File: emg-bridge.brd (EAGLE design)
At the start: 76.2 x 50.8 mm, 24 parts, among them J1 RJ25_4X1, J2 RJ25_4X1, J3 M03_0.156IN-RA, U1 ADM660ARZ

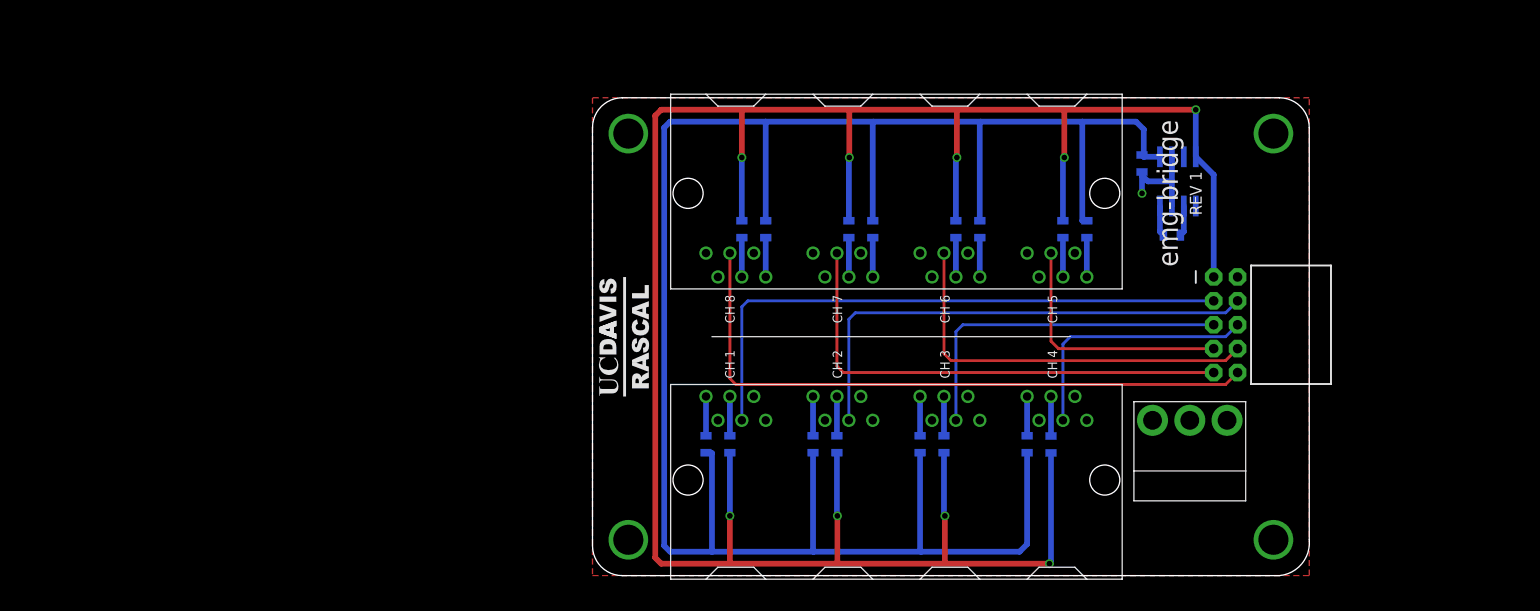
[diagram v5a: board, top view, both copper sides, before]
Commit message: Realization: the MC USB-1608G DAQ can only output 10mA for power, so the power circuitry has been completely reworked. Now with 3kV isolation!
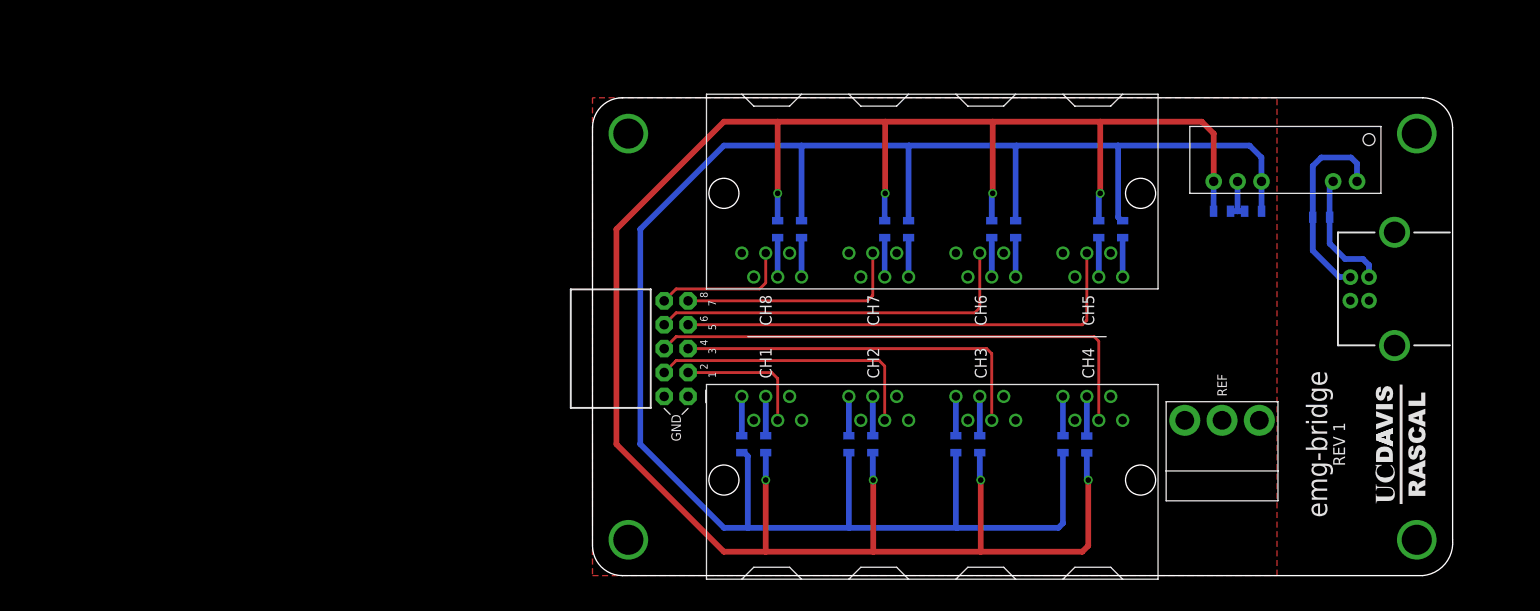
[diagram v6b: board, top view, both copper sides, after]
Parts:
- removed U1: ADM660ARZ, eagle-lib:SOIC8
- added C3: 0.1uF, SparkFun-Capacitors:0805
- added JP2: USB-B, SparkFun-Connectors:USB-B-PTH
- added U2: DC_ISOLATOR-RKZ0505D, eagle-lib:SIP7
- C1, C2: value 10uF -> 0.1uF
- moved U$1 83.3 mm to (86.0, 14.0)
- moved JP1 58.5 mm to (8.89, 24.1), turned to 180 degrees
- moved C1 16.0 mm to (77.5, 38.1), turned to 180 degrees
- moved C2 9.91 mm to (66.9, 38.7), turned to 180 degrees
- moved J2 3.81 mm to (58.3, 40.6)
- moved R10 3.81 mm to (56.4, 36.8)
- moved R12 3.81 mm to (45.0, 36.8)
- moved R16 3.81 mm to (22.2, 36.8)
- moved R4 3.81 mm to (27.3, 14.0)
- moved R5 3.81 mm to (41.2, 14.0)
- moved R6 3.81 mm to (38.6, 14.0)
- moved R8 3.81 mm to (50.0, 14.0)
- moved R9 3.81 mm to (53.8, 36.8)
- moved J1 3.81 mm to (14.0, 10.2)
- moved R2 3.81 mm to (15.9, 14.0)
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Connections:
- net +VE: now also C2.1, U2.7; no longer JP1.1, U1.8
- net -VE: now also C3.2, U2.5; no longer C2.1, U1.5
- net GND: now also C3.1, JP1.1, U2.6; no longer U1.3, U1.6
- net N$2: now also C1.1, JP2.VBUS, U2.1; no longer C1.2, U1.4
- net N$4: now also C1.2, JP2.GND, U2.2; no longer C1.1, U1.2
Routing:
- net CH8: track 68.1 -> 14.8 mm
- net CH1: track 62.5 -> 14.2 mm
- net CH7: track 52.4 -> 24.4 mm
- net CH4: track 27.5 -> 55.3 mm
- net CH2: track 52.9 -> 30.0 mm
- net CH5: track 27.0 -> 49.7 mm
- net +VE: track 260.1 -> 238.9 mm, vias 9 -> 8
- net N$2: track 3.25 -> 21.4 mm
- net -VE: track 224.8 -> 211.9 mm
- net N$4: track 3.25 -> 13.2 mm
- net GND: track 10.9 -> 4.68 mm, vias 1 -> 0
- net CH6: track 42.7 -> 40.1 mm
- net CH3: track 37.1 -> 39.6 mm
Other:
- board size 76.2 x 50.8 mm -> 91.5 x 50.8 mm
- board text added: "1"
- board text added: "2"
- board text added: "3"
- board text added: "4"
- board text added: "5"
- board text added: "6"
- board text added: "7"
- board text added: "8"
- board text added: "CH1"
- board text added: "CH2"
- board text added: "CH3"
- board text added: "CH4"
- board text added: "CH5"
- board text added: "CH6"
- board text added: "CH7"
- board text added: "CH8"
- board text added: "GND"
- board text added: "REF"
- board text removed: "CH 1"
- board text removed: "CH 2"
- board text removed: "CH 3"
- board text removed: "CH 4"
- board text removed: "CH 5"
- board text removed: "CH 6"
- board text removed: "CH 7"
- board text removed: "CH 8"

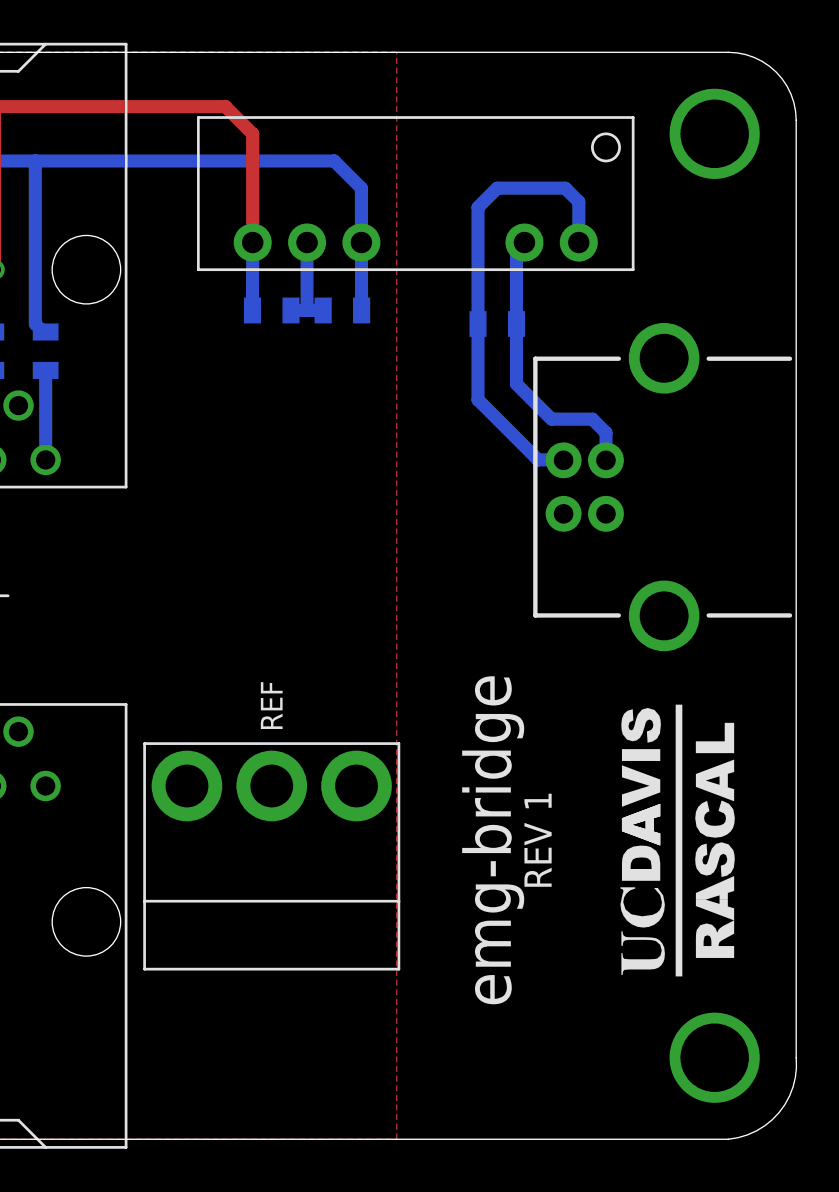
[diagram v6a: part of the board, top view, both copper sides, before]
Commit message: Added power jack.
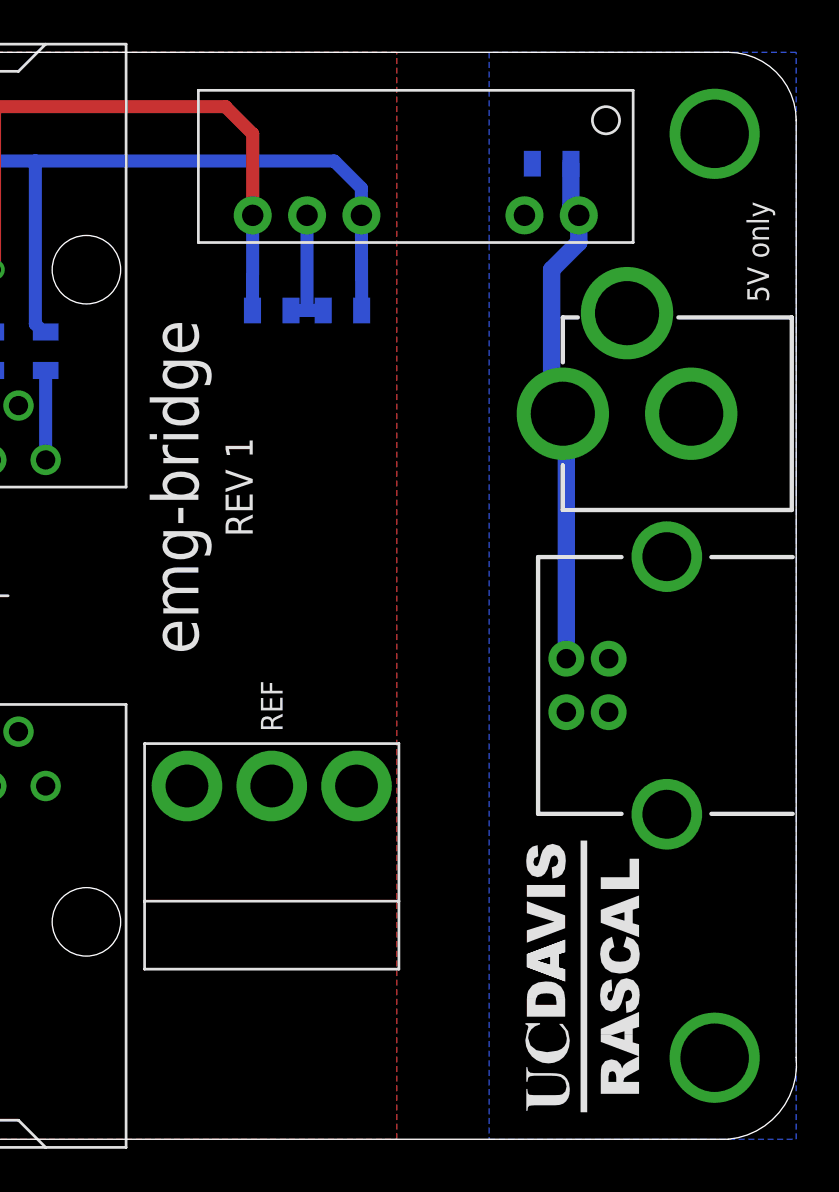
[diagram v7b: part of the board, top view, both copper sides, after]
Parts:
- removed JP2: USB-B, SparkFun-Connectors:USB-B-PTH
- removed U2: DC_ISOLATOR-RKZ0505D, eagle-lib:SIP7
- added J4: POWER_JACKPTH, SparkFun-Connectors:POWER_JACK_PTH
- added J5: USB-B, SparkFun-Connectors:USB-B-PTH
- added U1: DC_ISOLATOR-RKZ0505D, eagle-lib:SIP7
- moved C1 7.91 mm to (80.0, 45.6), turned to 0 degrees
- moved U$1 7.75 mm to (81.5, 7.62)
- renumbered JP1 to J6
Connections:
- removed net N$4: C1.2, JP2.GND, U2.2
- new net DGND: C1.2, J4.GND, J5.GND, U1.2
- net +VE: now also U1.7; no longer U2.7
- net -VE: now also U1.5; no longer U2.5
- net GND: now also U1.6; no longer U2.6
- net N$2: now also J4.PWR, J5.VBUS, U1.1; no longer JP2.VBUS, U2.1
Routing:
- net N$4: track 13.2 -> 0.00 mm
- net N$2: track 21.4 -> 24.1 mm
- net GND: track 4.68 -> 5.95 mm
- added copper zone on layer 16, net DGND
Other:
- board text added: "5V only"

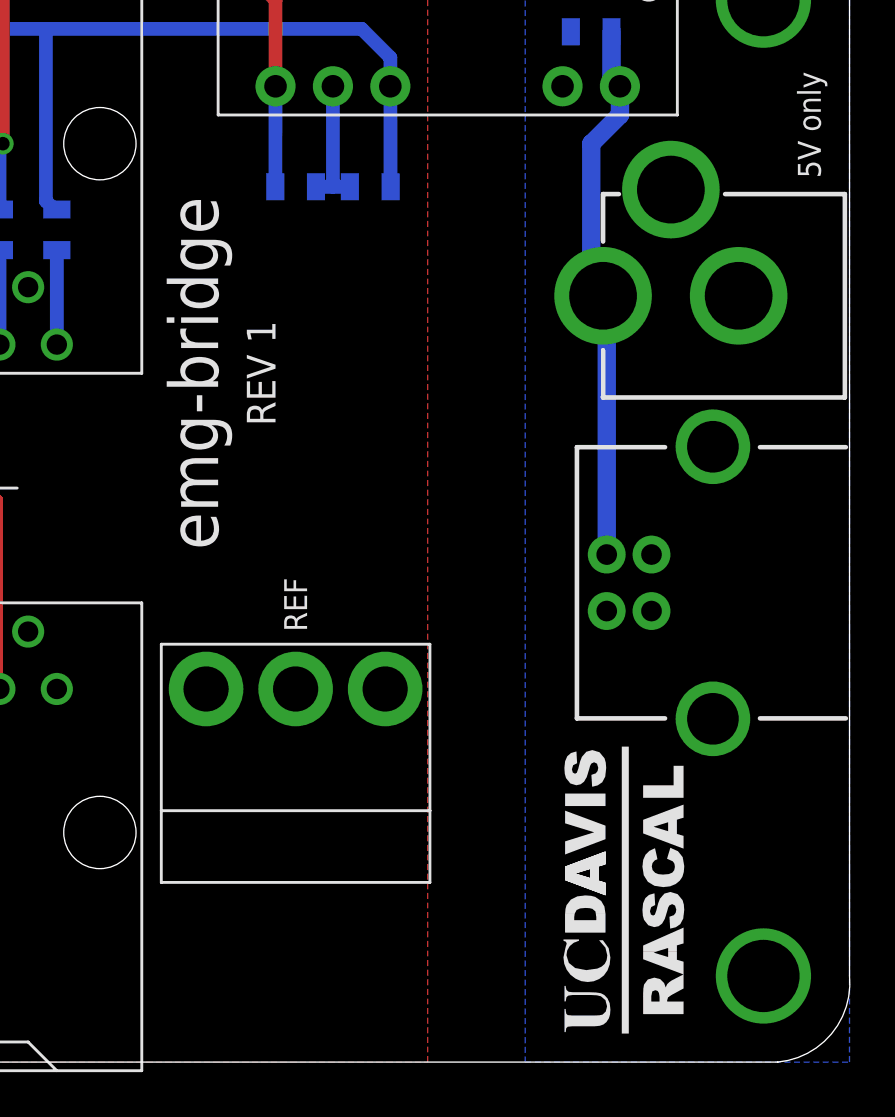
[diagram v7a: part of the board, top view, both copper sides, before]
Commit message: Added LED.
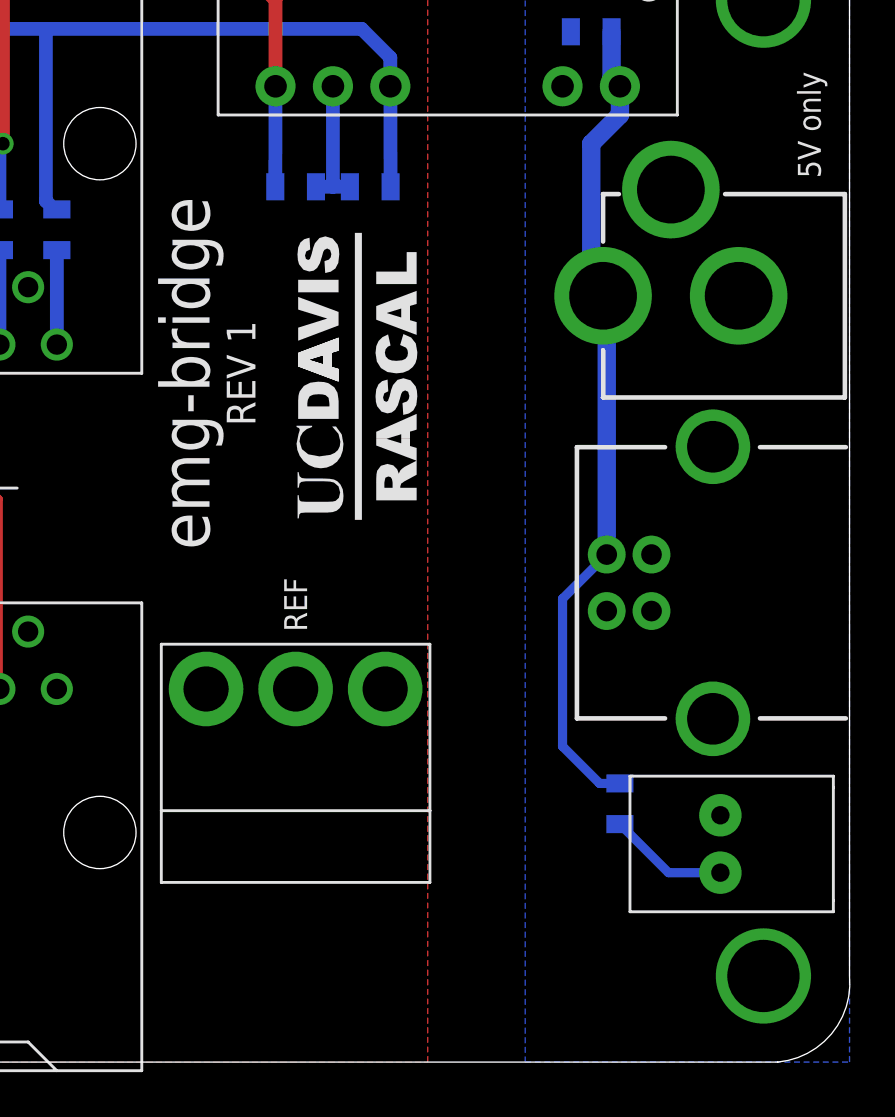
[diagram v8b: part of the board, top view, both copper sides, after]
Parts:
- added D1: LED_LA93B, eagle-lib:LED_RA
- added R17: (no value), SparkFun-Passives:0805
- moved U$1 25.6 mm to (69.7, 30.4)
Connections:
- new net N$4: D1.A, R17.1
- net DGND: now also D1.K
- net N$2: now also R17.2
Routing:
- net N$2: track 24.1 -> 36.6 mm
- net N$4: track 0.00 -> 5.33 mm
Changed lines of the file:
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@@
 <wire x1="3.175" y1="50.8" x2="0" y2="47.625" width="0" layer="20" curve="90"/>
 <wire x1="88.265" y1="50.8" x2="91.44" y2="47.625" width="0" layer="20" curve="-90"/>
-<text x="63.5" y="30.48" size="2.1844" layer="21" font="vector" ratio="15" rot="R90" align="bottom-center">emg-bridge</text>
-<text x="66.04" y="30.48" size="1.27" layer="21" font="vector" ratio="10" rot="R90" align="bottom-center">REV 1</text>
+<text x="63.119" y="30.48" size="2.1844" layer="21" font="vector" ratio="15" rot="R90" align="bottom-center">emg-bridge</text>
+<text x="65.151" y="30.48" size="1.27" layer="21" font="vector" ratio="10" rot="R90" align="bottom-center">REV 1</text>
 <text x="18.415" y="20.955" size="1.27" layer="21" font="vector" ratio="12" rot="R90" align="center-left">CH1</text>
 <text x="29.845" y="20.955" size="1.27" layer="21" font="vector" ratio="12" rot="R90" align="center-left">CH2</text>
@@
 <element name="J3" library="eagle-lib" package="TE_640389-3" value="M03_0.156IN-RA" x="66.929" y="16.51" smashed="yes" rot="R180"/>
 <element name="J6" library="SparkFun-Connectors" package="2X5-RAF" value="M05X2RAF" x="8.89" y="24.13" smashed="yes" rot="R180"/>
-<element name="U$1" library="ucdrascal-eagle-lib" package="UCDAVIS-RASCAL_LOGO" value="UCDAVIS-RASCAL_LOGO-2LINE" x="81.534" y="7.62" rot="R90"/>
+<element name="U$1" library="ucdrascal-eagle-lib" package="UCDAVIS-RASCAL_LOGO" value="UCDAVIS-RASCAL_LOGO-2LINE" x="69.723" y="30.353" rot="R90"/>
 <element name="U1" library="eagle-lib" package="SIP7" value="DC_ISOLATOR-RKZ0505D" x="81.28" y="43.18" rot="R180"/>
 <element name="J5" library="SparkFun-Connectors" package="USB-B-PTH" value="USB-B" x="82.677" y="21.209" smashed="yes" rot="R180">
@@
 </element>
 <element name="J4" library="SparkFun-Connectors" package="POWER_JACK_PTH" value="POWER_JACKPTH" x="94.234" y="33.909" smashed="yes" rot="R90"/>
+<element name="D1" library="eagle-lib" package="LED_RA" value="LED_LA93B" x="85.725" y="9.652" smashed="yes" rot="R90"/>
+<element name="R17" library="SparkFun-Passives" package="0805" value="" x="81.28" y="11.43" smashed="yes" rot="MR90">
+<attribute name="NAME" x="80.137" y="11.3665" size="0.4064" layer="26" rot="MR0"/>
+<attribute name="VALUE" x="79.883" y="10.414" size="0.4064" layer="28" rot="MR90"/>
+</element>
 </elements>
 <signals>
@@
 <vertex x="91.44" y="50.8"/>
 </polygon>
+<contactref element="D1" pad="K"/>
 </signal>
 <signal name="N$2">
@@
 <wire x1="80.01" y1="40.64" x2="80.01" y2="34.433" width="0.8128" layer="16"/>
 <wire x1="80.01" y1="34.433" x2="80.534" y2="33.909" width="0.8128" layer="16"/>
+<contactref element="R17" pad="2"/>
+<wire x1="81.28" y1="12.33" x2="80.38" y2="12.33" width="0.4064" layer="16"/>
+<wire x1="80.38" y1="12.33" x2="78.74" y2="13.97" width="0.4064" layer="16"/>
+<wire x1="78.74" y1="13.97" x2="78.74" y2="20.5032" width="0.4064" layer="16"/>
+<wire x1="78.74" y1="20.5032" x2="80.6958" y2="22.459" width="0.4064" layer="16"/>
+</signal>
+<signal name="N$4">
+<contactref element="R17" pad="1"/>
+<contactref element="D1" pad="A"/>
+<wire x1="85.725" y1="8.382" x2="83.428" y2="8.382" width="0.4064" layer="16"/>
+<wire x1="83.428" y1="8.382" x2="81.28" y2="10.53" width="0.4064" layer="16"/>
 </signal>
 </signals>
